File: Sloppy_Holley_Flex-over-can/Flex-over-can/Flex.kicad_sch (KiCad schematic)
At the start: 5 parts

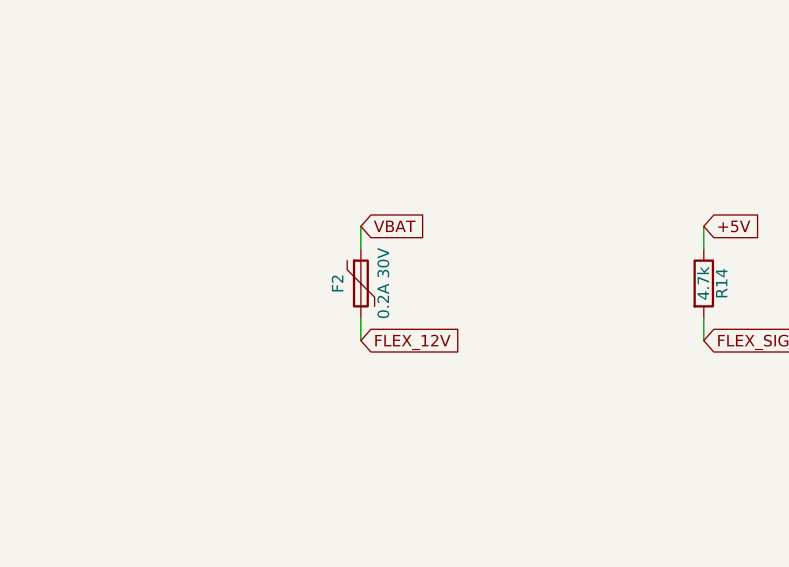
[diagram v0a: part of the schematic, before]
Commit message: Review power/connector sheets, fix ERC, add 3D models for all parts
- Remove duplicate PWR_FLAG on +5V (ERC pin_to_pin error)
- Register KiCad_Footprints and 24pinConnectorSymbol libs for J1
- Correct D1 value to B160-13-F and RV1 to SMDJ24CA to match LCSC parts
- C1: 10uF 50V X5R 1206 (C13585) for load-dump margin
- F2: 0.2A/60V resettable PTC, Brightking SMD1812B020TF-J (C269125)
- Add STEP models for J1, J2 (USB-C), SW1 (BOOT) and fix ESP32 model path
- Project-local footprint copies carry the models for J2, SW1, F2

Co-Authored-By: Claude Opus 5.5 <noreply@anthropic.com>
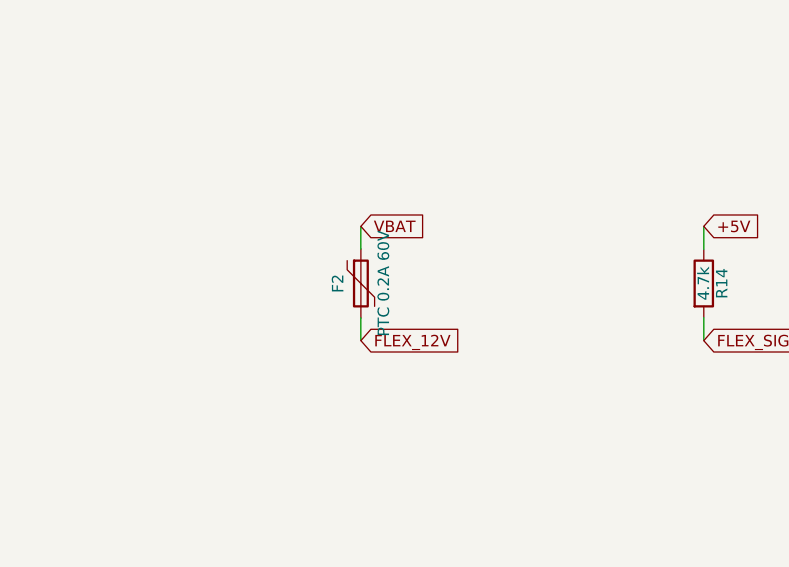
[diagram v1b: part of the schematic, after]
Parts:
- F2: value 0.2A 30V -> PTC 0.2A 60V; footprint Fuse:Fuse_1206_3216Metric -> KiCad_Footprints:Fuse_1812_4532Metric; LCSC C69680 -> C269125; MPN (none) -> SMD1812B020TF-J; URL (none) -> https://jlcpcb.com/partdetail/SMD1812B020TF-J/C269125
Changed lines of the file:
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@@
 			)
 		)
-		(property "Value" "0.2A 30V"
+		(property "Value" "PTC 0.2A 60V"
 			(at 66.04 76.2 90)
 			(show_name no)
@@
 			)
 		)
-		(property "Footprint" "Fuse:Fuse_1206_3216Metric"
+		(property "Footprint" "KiCad_Footprints:Fuse_1812_4532Metric"
 			(at 63.5 76.2 0)
 			(hide yes)
@@
 			)
 		)
-		(property "Datasheet" ""
+		(property "Datasheet" "https://www.lcsc.com/product-detail/C269125.html"
 			(at 63.5 76.2 0)
 			(hide yes)
@@
 			)
 		)
-		(property "Description" "Resettable fuse, polymeric positive temperature coefficient"
+		(property "Description" "PTC resettable fuse, 0.2A hold / 0.4A trip, 60V, 1812 (Brightking SMD1812B020TF-J)"
 			(at 63.5 76.2 0)
 			(hide yes)
@@
 			)
 		)
-		(property "LCSC" "C69680"
+		(property "LCSC" "C269125"
 			(at 63.5 76.2 0)
 			(hide yes)
@@
 			)
 		)
-	)
+		(property "MPN" "SMD1812B020TF-J"
+			(at 63.5 76.2 0)
+			(hide yes)
+			(effects
+				(font
+					(size 1.27 1.27)
+				)
+			)
+		)
+		(property "URL" "https://jlcpcb.com/partdetail/SMD1812B020TF-J/C269125"
+			(at 63.5 76.2 0)
+			(hide yes)
+			(effects
+				(font
+					(size 1.27 1.27)
+				)
+			)
+		))
 	(symbol
 		(lib_id "Device:R")

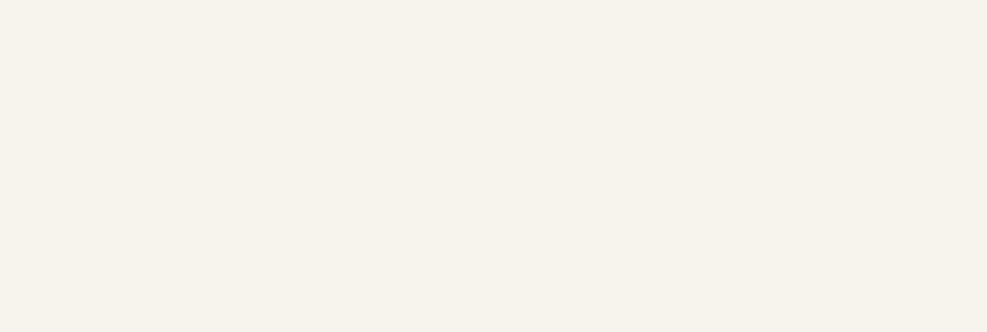
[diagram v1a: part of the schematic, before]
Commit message: Add PCB placement notes for decoupling caps to each sheet
Co-Authored-By: Claude Opus 5.5 <noreply@anthropic.com>
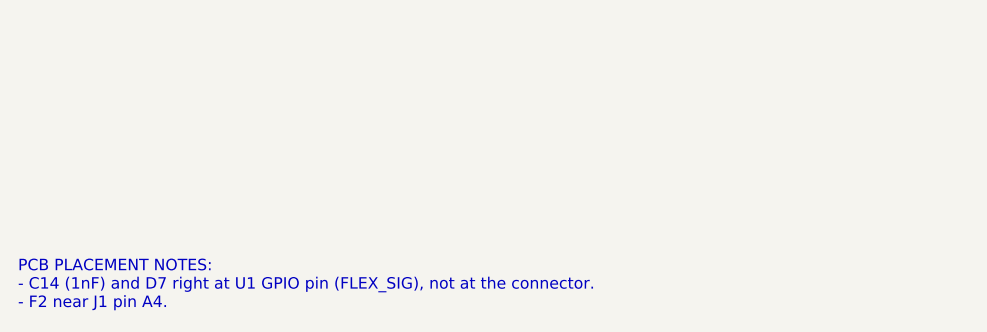
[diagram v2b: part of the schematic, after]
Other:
- note added: "PCB PLACEMENT NOTES: - C14 (1nF) and D7 right at U1 GPIO pin (FLEX_SIG), not at the connector. - F2 near J1 pin A4."
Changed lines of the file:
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@@
 		)
 	)
+  (text "PCB PLACEMENT NOTES:\n- C14 (1nF) and D7 right at U1 GPIO pin (FLEX_SIG), not at the connector.\n- F2 near J1 pin A4."
+    (at 15.24 180.34 0)
+    (effects (font (size 1.27 1.27) (color 0 0 194 1)) (justify left bottom))
+  )
 	(symbol
 		(lib_id "Device:Polyfuse")
